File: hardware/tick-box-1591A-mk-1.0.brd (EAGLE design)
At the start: 94 x 44 mm, 29 parts, among them IC2 DS3231, IC3 LM2931-5V, U1 ATMEGA328P_PDIP, Y1 16MHz

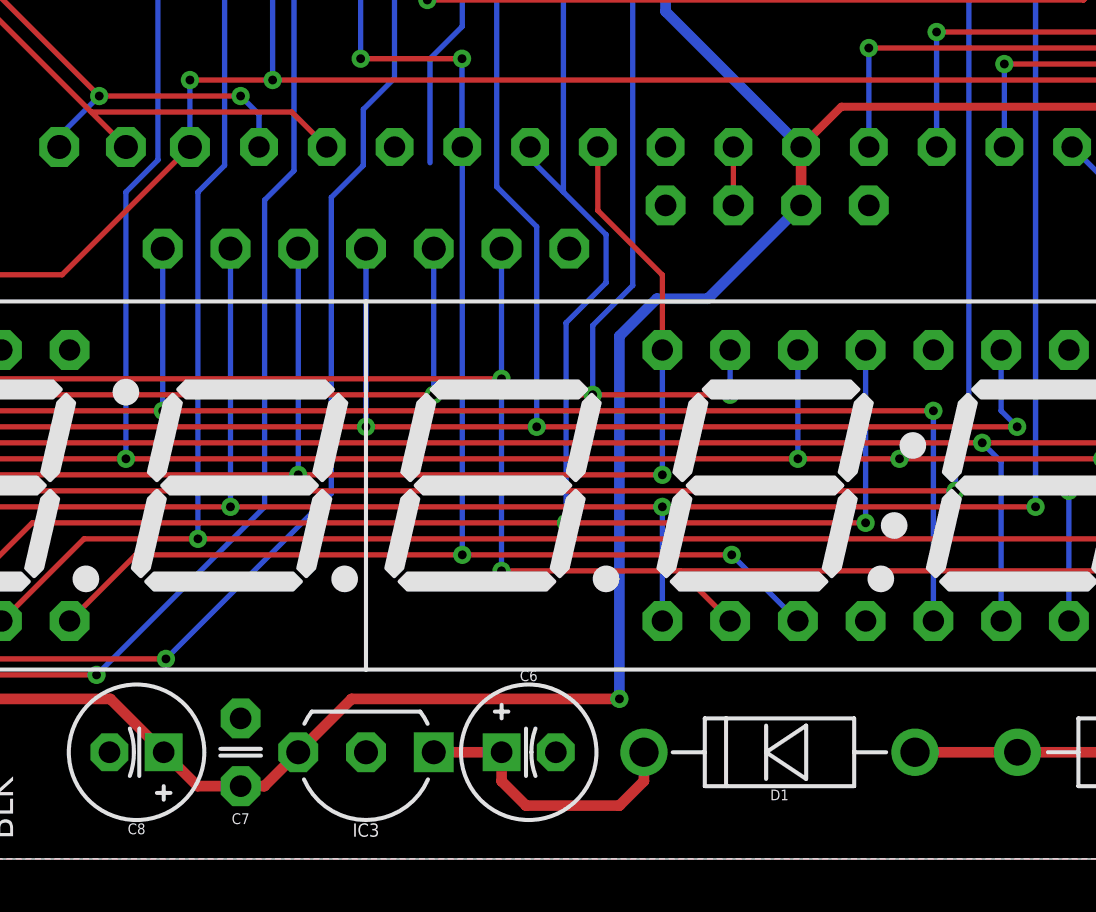
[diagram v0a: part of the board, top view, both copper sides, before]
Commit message: clocks are hard, some more stabs
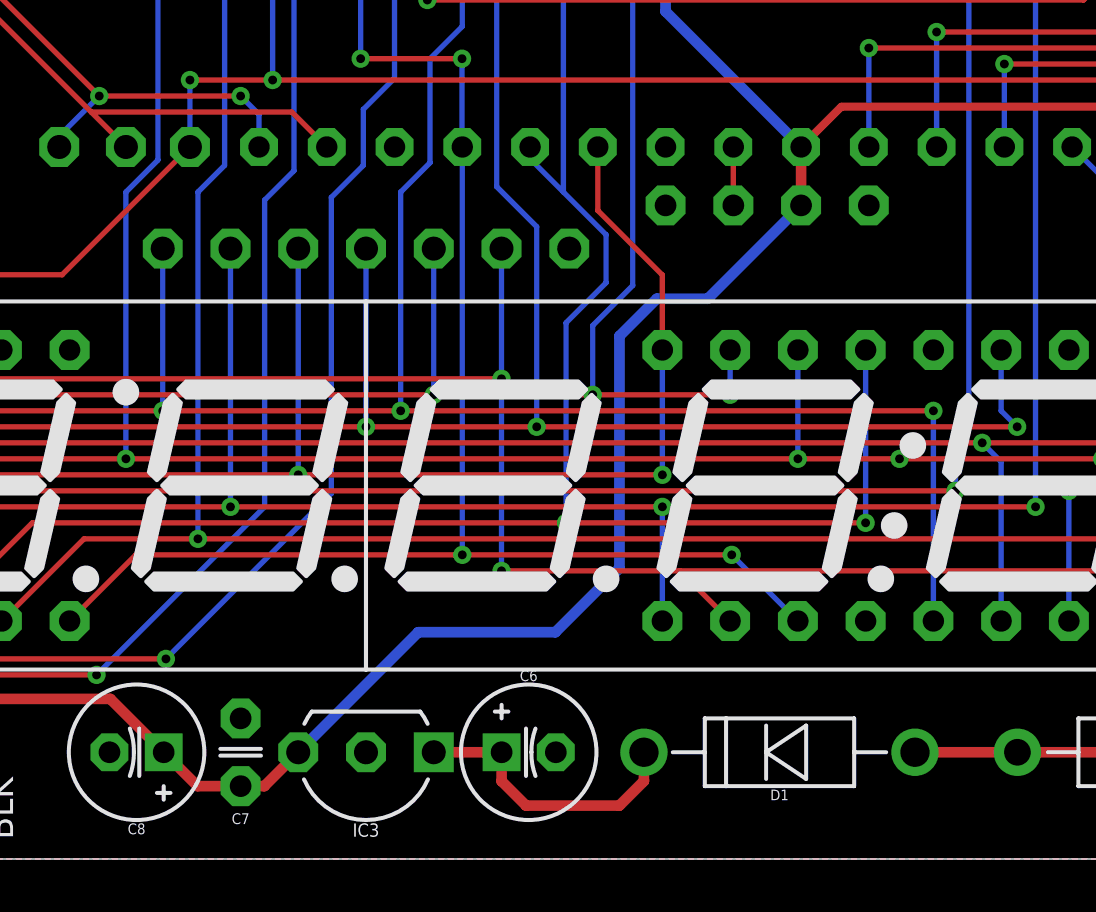
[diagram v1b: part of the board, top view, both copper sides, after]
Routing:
- net D2: track 68.7 -> 78.5 mm, vias 2 -> 3
- net VCC: track 157.8 -> 154.9 mm, vias 2 -> 1
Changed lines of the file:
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@@
 <setting verticaltext="up"/>
 </settings>
-<grid distance="0.1" unitdist="mm" unit="mm" style="lines" multiple="5" display="yes" altdistance="0.01" altunitdist="mm" altunit="mm"/>
+<grid distance="0.1" unitdist="mm" unit="mm" style="lines" multiple="5" display="yes" altdistance="1" altunitdist="mil" altunit="mil"/>
 <layers>
 <layer number="1" name="Top" color="4" fill="1" visible="yes" active="yes"/>
@@
 <element name="DISPLAY2" library="A_butts" package="7SEG_4DIG_10MM" value="7SEG_4DIGIT_COLON_APOS" x="67" y="14" locked="yes" smashed="yes"/>
 <element name="DISPLAY3" library="A_butts" package="7SEG_4DIG_10MM" value="7SEG_4DIGIT_COLON_APOS" x="27" y="14" locked="yes" smashed="yes"/>
-<element name="C1" library="A_butts" package="C025-024X044" value="1uF" x="64.58" y="24.5" rot="MR180"/>
+<element name="C1" library="A_butts" package="C025-024X044" value="1uF" x="64.58" y="24.5" smashed="yes" rot="MR180">
+<attribute name="NAME" x="64.6" y="25.506" size="0.4064" layer="26" font="vector" ratio="12" rot="MR0" align="bottom-center"/>
+<attribute name="VALUE" x="64.6" y="23.434" size="0.4064" layer="28" font="vector" ratio="12" rot="MR180" align="bottom-center"/>
+</element>
 <element name="C2" library="A_butts" package="C025-024X044" value="0.1uF" x="5.005" y="31.675" rot="R180"/>
 <element name="R2" library="A_butts" package="RESISTOR-AXIAL-PTH-7.62MM" value="4.7k" x="38" y="30.5" rot="MR270"/>
@@
 <element name="C3" library="A_butts" package="C025-024X044" value="22pF" x="58" y="40" locked="yes" rot="MR90"/>
 <element name="C4" library="A_butts" package="C025-024X044" value="22pF" x="71" y="40" locked="yes" rot="MR90"/>
-<element name="C5" library="A_butts" package="C025-024X044" value="0.1uF" x="59.5" y="24.5" rot="MR0"/>
+<element name="C5" library="A_butts" package="C025-024X044" value="0.1uF" x="59.5" y="24.5" smashed="yes" rot="MR0">
+<attribute name="NAME" x="59.5" y="25.486" size="0.4064" layer="26" font="vector" ratio="12" rot="MR0" align="bottom-center"/>
+<attribute name="VALUE" x="59.5" y="23.514" size="0.4064" layer="28" font="vector" ratio="12" rot="MR180" align="bottom-center"/>
+</element>
 <element name="RESET" library="A_butts" package="DTS-6-SMALL-PADS" value="SPST-NO-TACT6MM-PTH-SMALL-PADS" x="4.5" y="25.885" rot="R90"/>
 <element name="R1" library="A_butts" package="RESISTOR-AXIAL-PTH-7.62MM" value="10k" x="40.4" y="30.5" rot="MR270"/>
@@
 <wire x1="23.19" y1="19.08" x2="25.47" y2="16.8" width="0.2" layer="1"/>
 <wire x1="25.47" y1="16.8" x2="39.38" y2="16.8" width="0.2" layer="1"/>
-<wire x1="39.38" y1="16.8" x2="68.27" y2="16.8" width="0.2" layer="1"/>
+<wire x1="39.38" y1="16.8" x2="48.3" y2="16.8" width="0.2" layer="1"/>
+<wire x1="48.3" y1="16.8" x2="68.27" y2="16.8" width="0.2" layer="1"/>
 <wire x1="68.27" y1="16.8" x2="68.27" y2="8.92" width="0.2" layer="16"/>
 <via x="68.27" y="16.8" extent="1-16" drill="0.3302"/>
@@
 <wire x1="49.4" y1="30" x2="50.61" y2="31.21" width="0.2" layer="16"/>
 <wire x1="50.61" y1="31.21" x2="50.61" y2="34.31" width="0.2" layer="16"/>
-<wire x1="39.38" y1="22.88" x2="49.4" y2="26.1" width="0" layer="19" extent="16-16"/>
+<via x="48.3" y="16.8" extent="1-16" drill="0.3302"/>
+<wire x1="49.4" y1="26.1" x2="48.3" y2="25" width="0.2" layer="16"/>
+<wire x1="48.3" y1="25" x2="48.3" y2="16.8" width="0.2" layer="16"/>
 </signal>
 <signal name="A2">
@@
 <wire x1="44.46" y1="4" x2="43.19" y2="2.73" width="0.4" layer="1"/>
 <wire x1="43.19" y1="2.73" x2="42.3" y2="2.73" width="0.4" layer="1"/>
-<wire x1="44.46" y1="4" x2="46.46" y2="6" width="0.4" layer="1"/>
 <wire x1="6.275" y1="31.675" x2="8" y2="31.675" width="0.3" layer="1"/>
 <wire x1="8" y1="31.675" x2="9.815" y2="31.675" width="0.3" layer="1"/>
@@
 <wire x1="8.81" y1="34.31" x2="8" y2="33.5" width="0.3" layer="1"/>
 <wire x1="8" y1="33.5" x2="8" y2="31.675" width="0.3" layer="1"/>
-<wire x1="46.46" y1="6" x2="56.5" y2="6" width="0.4" layer="1"/>
-<wire x1="56.5" y1="6" x2="56.5" y2="19.6" width="0.4" layer="16"/>
-<via x="56.5" y="6" extent="1-16" drill="0.3302"/>
+<wire x1="56.5" y1="10.9" x2="56.5" y2="19.6" width="0.4" layer="16"/>
 <wire x1="56.5" y1="19.6" x2="57.9" y2="21" width="0.4" layer="16"/>
 <wire x1="57.9" y1="21" x2="59.81" y2="21" width="0.4" layer="16"/>
@@
 <wire x1="75.9" y1="38.9" x2="77.27" y2="40.27" width="0.3" layer="16"/>
 <wire x1="77.27" y1="40.27" x2="77.46" y2="40.27" width="0.3" layer="16"/>
+<wire x1="56.5" y1="10.9" x2="54.1" y2="8.5" width="0.4" layer="16"/>
+<wire x1="54.1" y1="8.5" x2="48.96" y2="8.5" width="0.4" layer="16"/>
+<wire x1="48.96" y1="8.5" x2="44.46" y2="4" width="0.4" layer="16"/>
 </signal>
 <signal name="GND">
